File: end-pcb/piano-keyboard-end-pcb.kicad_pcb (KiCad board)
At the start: 2 copper layers, 41.1 x 82 mm, 24 parts, among them J1 Conn_01x03_Male, J2 Conn_01x01_Male, J3 Conn_01x02_Male, J4 Conn_01x02_Male, J5 Conn_01x05_Female, J6 AudioJack2, SW1 SW_Push, SW2 SW_Push, SW3 SW_Push, SW4 SW_Push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

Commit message: make end PCB use Teensy pin 9 instead of MOSI, to match the software
Also move the Teensy down to make room for the new connection, and
reroute traces and rearrange silkscreen to compensate. Also add the
github URL where this repo will be to the silkscreen.
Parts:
- added J5: Conn_01x01_Male, Connector_PinHeader_2.54mm:PinHeader_1x01_P2.54mm_Vertical, F.Cu at (97.8, 39.4)
- J4: value Conn_01x02_Male -> Conn_01x01_Male; footprint Connector_PinHeader_2.54mm:PinHeader_1x02_P2.54mm_Vertical -> Connector_PinHeader_2.54mm:PinHeader_1x01_P2.54mm_Vertical
- moved REF** 20.8 mm to (111.8, 81.3)
- moved J1 2.54 mm to (113.0, 47.0)
- moved J3 2.54 mm to (105.4, 47.0)
- moved J4 2.54 mm to (97.8, 47.0), turned to 0 degrees
- moved R1 2.54 mm to (94.5, 41.9)
- moved R2 2.54 mm to (94.5, 54.6)
- moved R3 2.54 mm to (102.1, 50.8)
- renumbered J5 to J6, J6 to J7
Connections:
- J6 pad 4: /MOSI-SHIFT -> /9-SHIFT
- U1 pad 1: /MOSI-SHIFT -> /9-SHIFT
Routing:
- net /9-SHIFT: track 0.00 -> 58.5 mm, vias 0 -> 2
- net /MOSI-SHIFT: track 55.9 -> 0.00 mm, vias 2 -> 0
- net /CLOCK: track 59.1 -> 56.6 mm
- net +3V3: track 87.7 -> 85.1 mm
- net /A0-PITCH: track 114.8 -> 117.3 mm
- net Net-(RN1-Pad6): track 75.5 -> 73.8 mm
- net Net-(RN1-Pad9): track 68.8 -> 70.6 mm
- net /A1-MOD: track 69.5 -> 71.3 mm
- net Net-(RN1-Pad7): track 80.9 -> 79.2 mm
- net Net-(RN1-Pad5): track 67.6 -> 68.8 mm
- net Net-(R1-Pad1): track 19.8 -> 20.6 mm
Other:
- board text added: "3V3"
- board text added: "9"
- board text added: "A0"
- board text added: "A1"
- board text added: "MISO"
- board text added: "SCK"
- board text added: "github.com/wdebeaum/piano-keyboard"

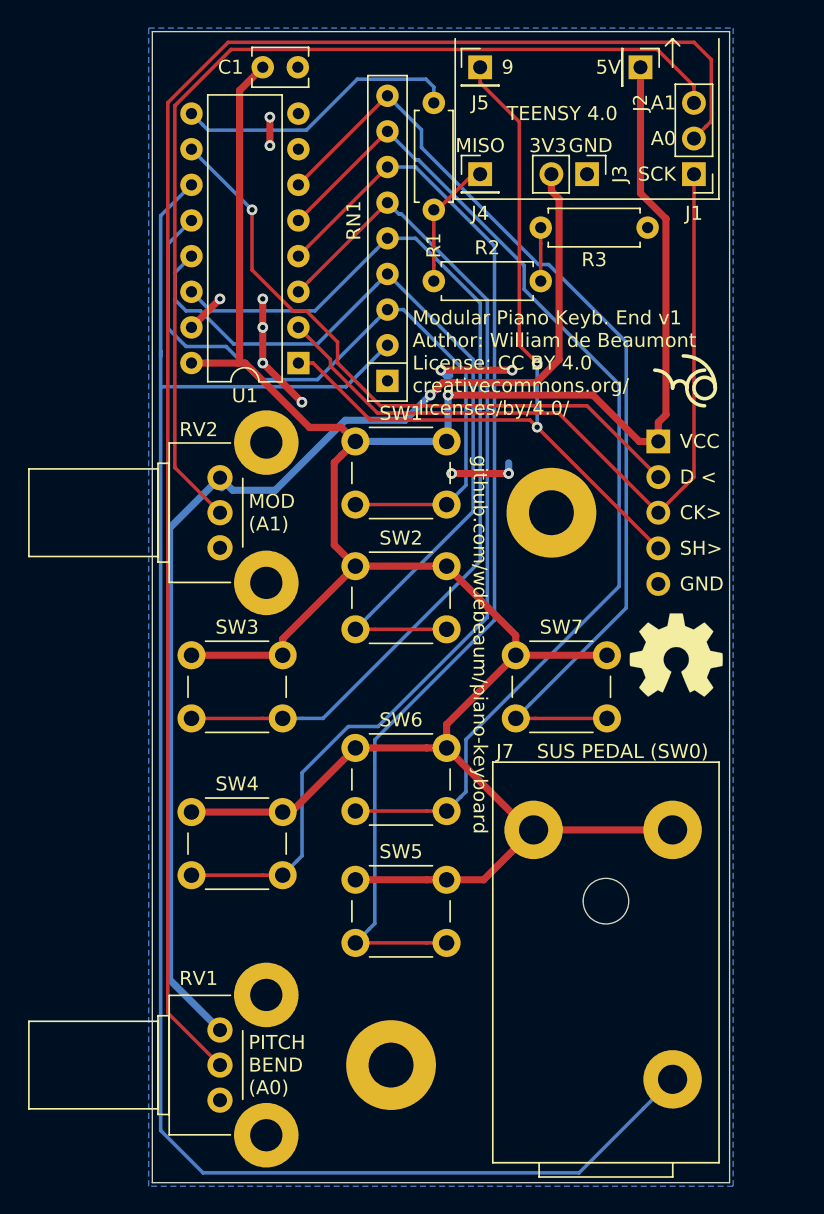
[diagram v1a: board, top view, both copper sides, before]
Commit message: use 3.3V throughout, instead of mixing it with 5V levels
This fixes the issues with the highest few keys intermittently not
working. It also makes the end PCB a little simpler. The shift registers
won't run as fast, but it turns out they don't need to.
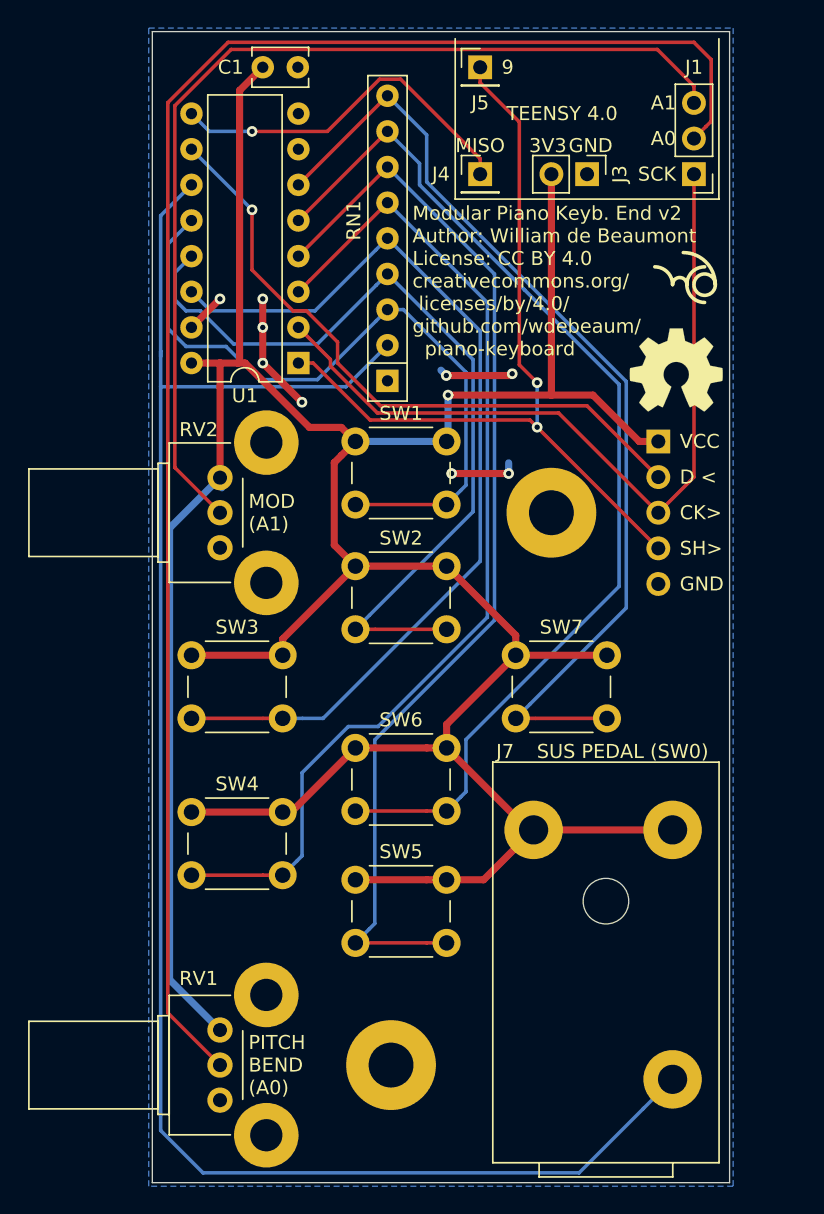
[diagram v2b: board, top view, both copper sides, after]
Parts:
- removed J2: Conn_01x01_Male, Connector_PinHeader_2.54mm:PinHeader_1x01_P2.54mm_Vertical
- removed R1, R2, R3: 10k, Resistor_THT:R_Axial_DIN0207_L6.3mm_D2.5mm_P7.62mm_Horizontal
- moved REF** 20.3 mm to (111.8, 61.0)
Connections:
- J3 pad 2: +3V3 -> VCC
- RV1 pad : GND -> (no net)
- RV1 pad 1: +3V3 -> VCC
- RV2 pad : GND -> (no net)
- RV2 pad 1: +3V3 -> VCC
- U1 pad 9: Net-(R1-Pad1) -> /MISO-DATA_OUT
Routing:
- net +3V3: track 85.1 -> 0.00 mm, vias 1 -> 0
- net VCC: track 197.6 -> 237.1 mm
- net Net-(R1-Pad1): track 20.6 -> 0.00 mm
- net /MISO-DATA_OUT: track 9.18 -> 26.1 mm, vias 0 -> 1
- net Net-(R2-Pad2): track 3.81 -> 0.00 mm
- net GND: track 24.2 -> 21.8 mm, vias 11 -> 9
- net Net-(RN1-Pad7): track 79.2 -> 78.0 mm
- net Net-(RN1-Pad5): track 68.8 -> 67.6 mm
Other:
- board text added: "Modular Piano Keyb. End v2 Author: William de Beaumont License: CC BY 4.0 creativecommons.org/ licenses/by/4.0/ github.com/wdebeaum/ piano-keyboard"
- board text removed: "5V"
- board text removed: "Modular Piano Keyb. End v1 Author: William de Beaumont License: CC BY 4.0 creativecommons.org/ licenses/by/4.0/"
- board text removed: "github.com/wdebeaum/piano-keyboard"
